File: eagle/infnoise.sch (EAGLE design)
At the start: 27 parts, among them SW1 MC74VHC1G66DFT1G, SW2 MC74VHC1G66DFT1G, X1 USBSMT-MALE

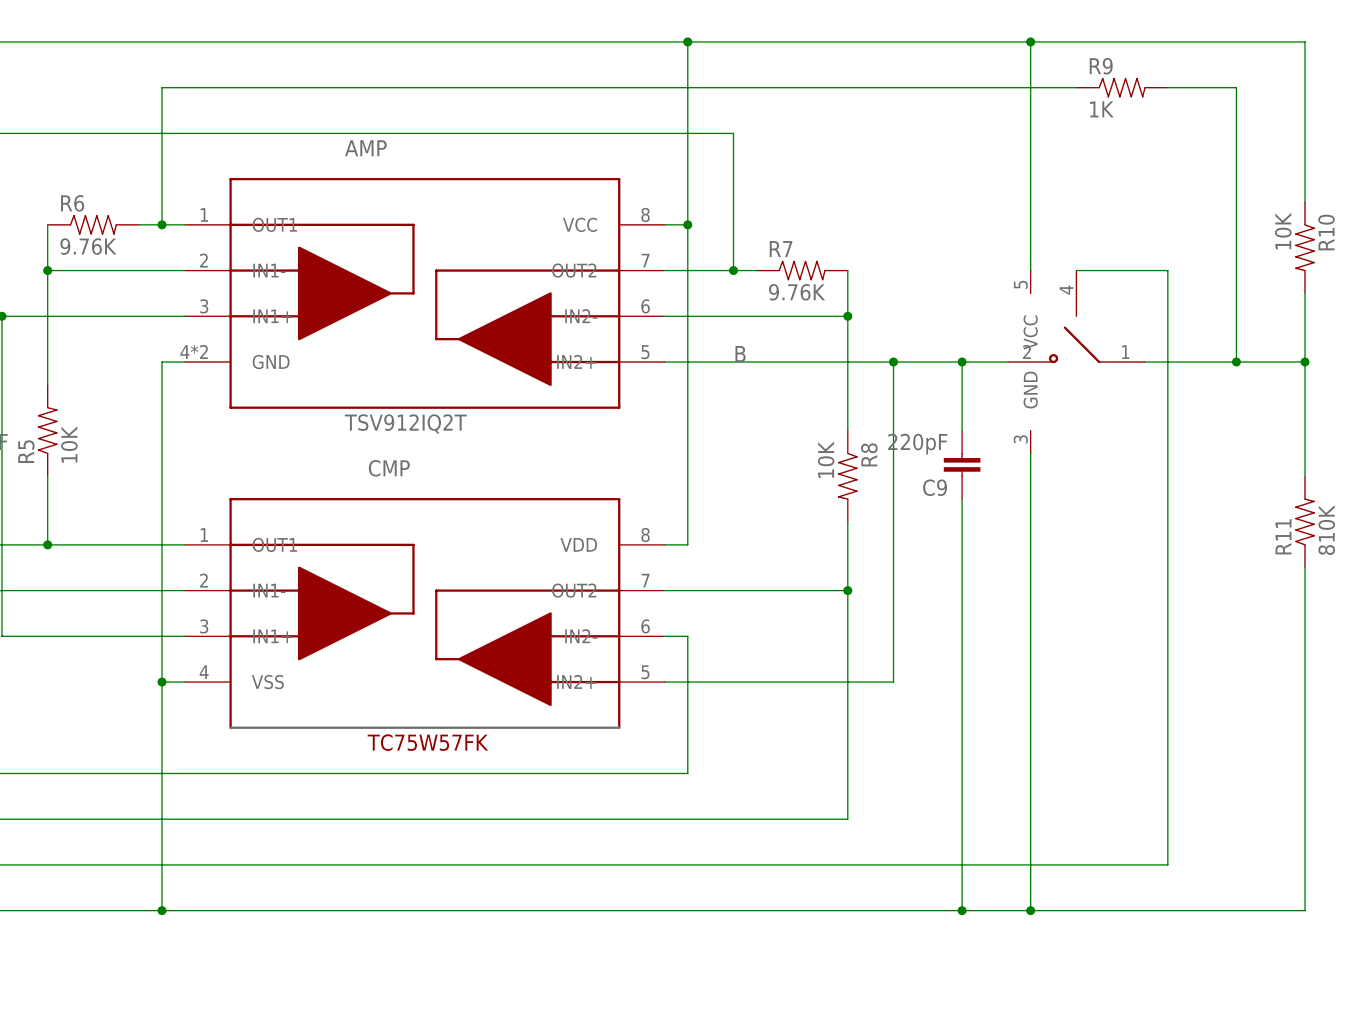
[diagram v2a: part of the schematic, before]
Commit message: Modified board to remove resistor in feedback, as well as pull-down
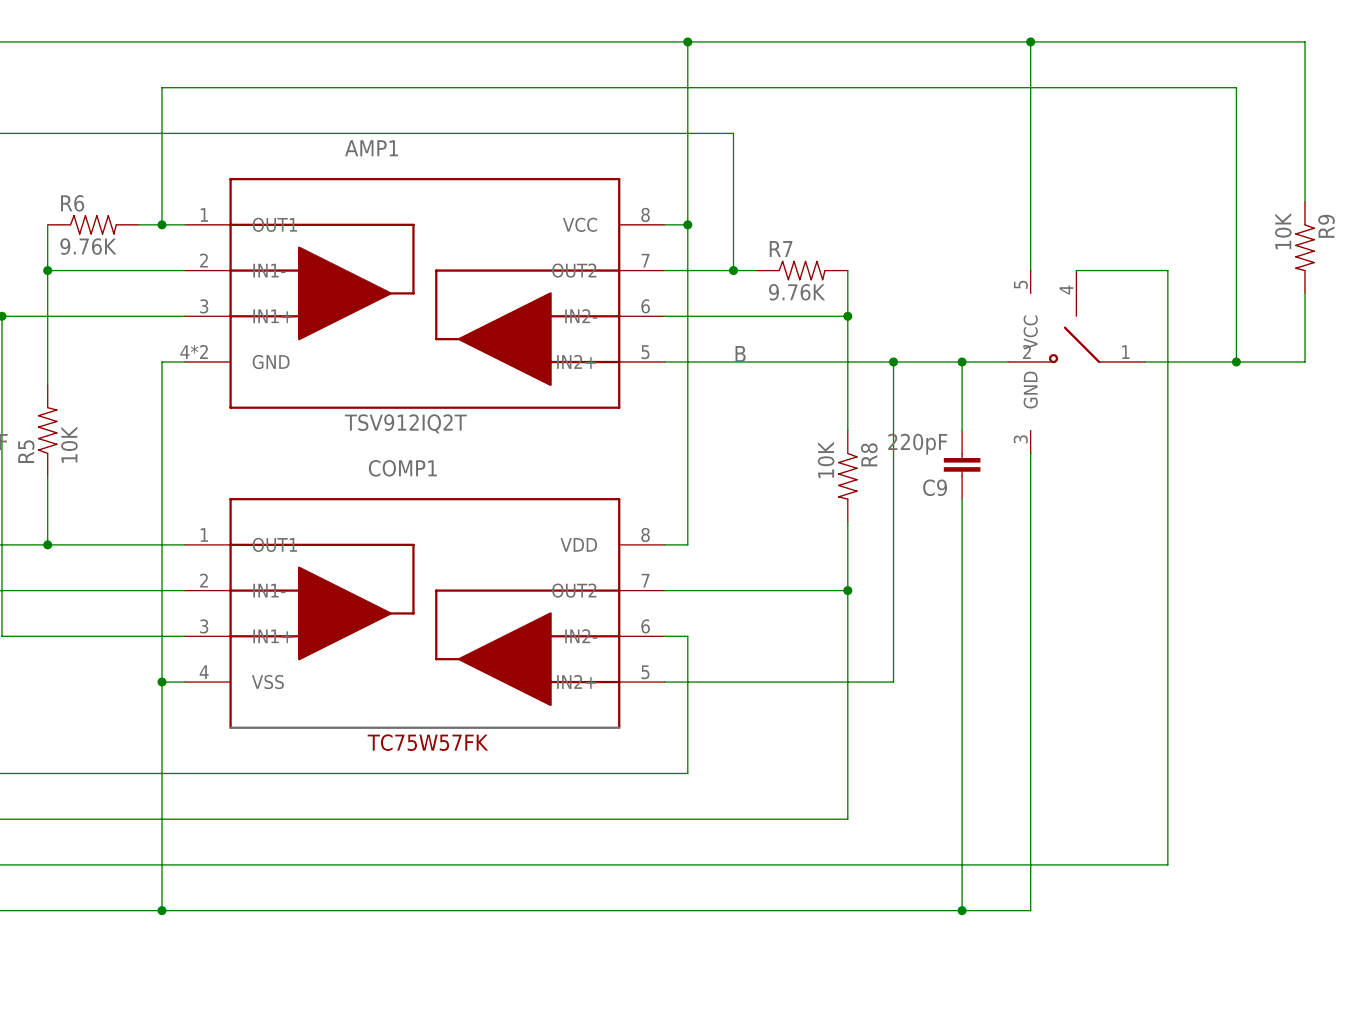
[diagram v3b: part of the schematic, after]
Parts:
- removed R10: 10K, infnoise:RESISTOR0603-RES
- removed R11: 810K, infnoise:RESISTOR0603-RES
- R9: value 1K -> 10K
- renumbered AMP to AMP1, CMP to COMP1
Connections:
- removed net N$1: AMP1.OUT1, R6.2, R9.1
- net AMP1OUT: now also AMP1.OUT1, R6.2; no longer R10.2, R11.2
- net GND: no longer R11.1
- net VCC33: now also R9.1; no longer R10.1
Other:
- moved on the sheet: R9
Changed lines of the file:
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@@
 <part name="R3" library="infnoise" deviceset="RESISTOR" device="0603-RES" value="10K"/>
 <part name="R4" library="infnoise" deviceset="RESISTOR" device="0603-RES" value="10K"/>
-<part name="AMP" library="infnoise" deviceset="TSV912" device="IQ2T"/>
-<part name="CMP" library="infnoise" deviceset="TC75W57" device="FK"/>
+<part name="AMP1" library="infnoise" deviceset="TSV912" device="IQ2T"/>
+<part name="COMP1" library="infnoise" deviceset="TC75W57" device="FK"/>
 <part name="SUPPLY1" library="supply2" deviceset="GND" device=""/>
-<part name="R10" library="infnoise" deviceset="RESISTOR" device="0603-RES" value="10K"/>
-<part name="R11" library="infnoise" deviceset="RESISTOR" device="0603-RES" value="810K"/>
+<part name="R9" library="infnoise" deviceset="RESISTOR" device="0603-RES" value="10K"/>
 <part name="SW1" library="infnoise" deviceset="MC74VHC1G66" device="DFT1G"/>
 <part name="SW2" library="infnoise" deviceset="MC74VHC1G66" device="DFT1G"/>
 <part name="X1" library="infnoise" deviceset="USB" device="SMT-MALE"/>
-<part name="R9" library="infnoise" deviceset="RESISTOR" device="0603-RES" value="1K"/>
 <part name="C7" library="infnoise" deviceset="CAP" device="0603-CAP" value="10nF"/>
 </parts>
@@
 <instance part="R3" gate="G$1" x="119.38" y="30.48" rot="R270"/>
 <instance part="R4" gate="G$1" x="119.38" y="10.16" rot="R270"/>
-<instance part="AMP" gate="G$1" x="208.28" y="50.8"/>
-<instance part="CMP" gate="G$1" x="208.28" y="15.24"/>
+<instance part="AMP1" gate="G$1" x="208.28" y="50.8"/>
+<instance part="COMP1" gate="G$1" x="208.28" y="15.24"/>
 <instance part="SUPPLY1" gate="GND" x="66.04" y="-20.32"/>
-<instance part="R10" gate="G$1" x="307.34" y="58.42" rot="R270"/>
-<instance part="R11" gate="G$1" x="307.34" y="27.94" rot="R90"/>
+<instance part="R9" gate="G$1" x="307.34" y="58.42" rot="R270"/>
 <instance part="SW1" gate="G$1" x="142.24" y="50.8"/>
 <instance part="SW2" gate="G$1" x="281.94" y="45.72" rot="MR0"/>
 <instance part="X1" gate="G$1" x="-43.18" y="35.56" rot="R180"/>
-<instance part="R9" gate="G$1" x="287.02" y="76.2"/>
 <instance part="C7" gate="G$1" x="132.08" y="7.62"/>
 </instances>
@@
 <wire x1="154.94" y1="35.56" x2="154.94" y2="-15.24" width="0.1524" layer="91"/>
 <wire x1="147.32" y1="40.64" x2="147.32" y2="-15.24" width="0.1524" layer="91"/>
-<pinref part="AMP" gate="G$1" pin="GND"/>
+<pinref part="AMP1" gate="G$1" pin="GND"/>
 <wire x1="182.88" y1="45.72" x2="180.34" y2="45.72" width="0.1524" layer="91"/>
 <wire x1="180.34" y1="45.72" x2="180.34" y2="10.16" width="0.1524" layer="91"/>
-<pinref part="CMP" gate="G$1" pin="VSS"/>
+<pinref part="COMP1" gate="G$1" pin="VSS"/>
 <wire x1="180.34" y1="10.16" x2="180.34" y2="-15.24" width="0.1524" layer="91"/>
 <wire x1="182.88" y1="10.16" x2="180.34" y2="10.16" width="0.1524" layer="91"/>
-<wire x1="276.86" y1="-15.24" x2="307.34" y2="-15.24" width="0.1524" layer="91"/>
-<pinref part="R11" gate="G$1" pin="1"/>
-<wire x1="307.34" y1="-15.24" x2="307.34" y2="22.86" width="0.1524" layer="91"/>
 <pinref part="SW1" gate="G$1" pin="GND"/>
 <pinref part="SW2" gate="G$1" pin="GND"/>
@@
 <junction x="154.94" y="-15.24"/>
 <junction x="180.34" y="-15.24"/>
-<junction x="276.86" y="-15.24"/>
 <junction x="15.24" y="10.16"/>
 <junction x="180.34" y="10.16"/>
@@
 <wire x1="147.32" y1="60.96" x2="147.32" y2="81.28" width="0.1524" layer="91"/>
 <wire x1="147.32" y1="81.28" x2="238.76" y2="81.28" width="0.1524" layer="91"/>
-<pinref part="CMP" gate="G$1" pin="VDD"/>
+<pinref part="COMP1" gate="G$1" pin="VDD"/>
 <wire x1="238.76" y1="81.28" x2="276.86" y2="81.28" width="0.1524" layer="91"/>
 <wire x1="276.86" y1="81.28" x2="307.34" y2="81.28" width="0.1524" layer="91"/>
 <wire x1="236.22" y1="25.4" x2="238.76" y2="25.4" width="0.1524" layer="91"/>
 <wire x1="238.76" y1="25.4" x2="238.76" y2="60.96" width="0.1524" layer="91"/>
-<pinref part="AMP" gate="G$1" pin="VCC"/>
+<pinref part="AMP1" gate="G$1" pin="VCC"/>
 <wire x1="238.76" y1="60.96" x2="238.76" y2="81.28" width="0.1524" layer="91"/>
 <wire x1="236.22" y1="60.96" x2="238.76" y2="60.96" width="0.1524" layer="91"/>
@@
 <wire x1="119.38" y1="35.56" x2="119.38" y2="81.28" width="0.1524" layer="91"/>
 <junction x="119.38" y="81.28"/>
-<pinref part="R10" gate="G$1" pin="1"/>
+<pinref part="R9" gate="G$1" pin="1"/>
 <wire x1="307.34" y1="81.28" x2="307.34" y2="63.5" width="0.1524" layer="91"/>
 <label x="58.42" y="81.28" size="1.778" layer="95"/>
@@
 <net name="A" class="0">
 <segment>
-<pinref part="AMP" gate="G$1" pin="IN1+"/>
+<pinref part="AMP1" gate="G$1" pin="IN1+"/>
 <wire x1="182.88" y1="50.8" x2="162.56" y2="50.8" width="0.1524" layer="91"/>
 <pinref part="C8" gate="G$1" pin="1"/>
@@
 <wire x1="154.94" y1="50.8" x2="149.86" y2="50.8" width="0.1524" layer="91"/>
 <wire x1="154.94" y1="43.18" x2="154.94" y2="50.8" width="0.1524" layer="91"/>
-<pinref part="CMP" gate="G$1" pin="IN1+"/>
+<pinref part="COMP1" gate="G$1" pin="IN1+"/>
 <wire x1="182.88" y1="15.24" x2="162.56" y2="15.24" width="0.1524" layer="91"/>
 <wire x1="162.56" y1="15.24" x2="162.56" y2="50.8" width="0.1524" layer="91"/>
@@
 <pinref part="SW2" gate="G$1" pin="COM"/>
 <wire x1="289.56" y1="45.72" x2="299.72" y2="45.72" width="0.1524" layer="91"/>
-<pinref part="R11" gate="G$1" pin="2"/>
 <wire x1="299.72" y1="45.72" x2="307.34" y2="45.72" width="0.1524" layer="91"/>
-<wire x1="307.34" y1="33.02" x2="307.34" y2="45.72" width="0.1524" layer="91"/>
 <wire x1="299.72" y1="76.2" x2="299.72" y2="45.72" width="0.1524" layer="91"/>
 <junction x="299.72" y="45.72"/>
-<pinref part="R10" gate="G$1" pin="2"/>
+<pinref part="R9" gate="G$1" pin="2"/>
 <wire x1="307.34" y1="53.34" x2="307.34" y2="45.72" width="0.1524" layer="91"/>
-<junction x="307.34" y="45.72"/>
-<pinref part="R9" gate="G$1" pin="2"/>
-<wire x1="292.1" y1="76.2" x2="299.72" y2="76.2" width="0.1524" layer="91"/>
+<pinref part="R6" gate="G$1" pin="2"/>
+<pinref part="AMP1" gate="G$1" pin="OUT1"/>
+<wire x1="182.88" y1="60.96" x2="180.34" y2="60.96" width="0.1524" layer="91"/>
+<wire x1="180.34" y1="60.96" x2="177.8" y2="60.96" width="0.1524" layer="91"/>
+<junction x="180.34" y="60.96"/>
+<wire x1="180.34" y1="60.96" x2="180.34" y2="76.2" width="0.1524" layer="91"/>
+<wire x1="180.34" y1="76.2" x2="299.72" y2="76.2" width="0.1524" layer="91"/>
 </segment>
 </net>
 <net name="FB1" class="0">
 <segment>
-<pinref part="AMP" gate="G$1" pin="IN1-"/>
+<pinref part="AMP1" gate="G$1" pin="IN1-"/>
 <wire x1="182.88" y1="55.88" x2="167.64" y2="55.88" width="0.1524" layer="91"/>
 <wire x1="167.64" y1="55.88" x2="167.64" y2="60.96" width="0.1524" layer="91"/>
@@
 <wire x1="132.08" y1="50.8" x2="134.62" y2="50.8" width="0.1524" layer="91"/>
 <pinref part="SW1" gate="G$1" pin="COM"/>
-<pinref part="AMP" gate="G$1" pin="OUT2"/>
+<pinref part="AMP1" gate="G$1" pin="OUT2"/>
 <pinref part="R7" gate="G$1" pin="1"/>
 <wire x1="246.38" y1="55.88" x2="243.84" y2="55.88" width="0.1524" layer="91"/>
@@
 <segment>
 <pinref part="R7" gate="G$1" pin="2"/>
-<pinref part="AMP" gate="G$1" pin="IN2-"/>
+<pinref part="AMP1" gate="G$1" pin="IN2-"/>
 <wire x1="236.22" y1="50.8" x2="256.54" y2="50.8" width="0.1524" layer="91"/>
 <wire x1="256.54" y1="50.8" x2="256.54" y2="55.88" width="0.1524" layer="91"/>
@@
 <net name="B" class="0">
 <segment>
-<pinref part="AMP" gate="G$1" pin="IN2+"/>
+<pinref part="AMP1" gate="G$1" pin="IN2+"/>
 <wire x1="274.32" y1="45.72" x2="269.24" y2="45.72" width="0.1524" layer="91"/>
 <wire x1="269.24" y1="45.72" x2="261.62" y2="45.72" width="0.1524" layer="91"/>
 <wire x1="261.62" y1="45.72" x2="236.22" y2="45.72" width="0.1524" layer="91"/>
-<pinref part="CMP" gate="G$1" pin="IN2+"/>
+<pinref part="COMP1" gate="G$1" pin="IN2+"/>
 <wire x1="236.22" y1="10.16" x2="261.62" y2="10.16" width="0.1524" layer="91"/>
 <wire x1="261.62" y1="10.16" x2="261.62" y2="45.72" width="0.1524" layer="91"/>
@@
 <net name="COMP1" class="0">
 <segment>
-<pinref part="CMP" gate="G$1" pin="OUT1"/>
+<pinref part="COMP1" gate="G$1" pin="OUT1"/>
 <wire x1="182.88" y1="25.4" x2="167.64" y2="25.4" width="0.1524" layer="91"/>
 <wire x1="167.64" y1="25.4" x2="127" y2="25.4" width="0.1524" layer="91"/>
@@
 <net name="COMP2" class="0">
 <segment>
-<pinref part="CMP" gate="G$1" pin="OUT2"/>
+<pinref part="COMP1" gate="G$1" pin="OUT2"/>
 <wire x1="236.22" y1="20.32" x2="256.54" y2="20.32" width="0.1524" layer="91"/>
 <wire x1="256.54" y1="20.32" x2="256.54" y2="-5.08" width="0.1524" layer="91"/>
@@
 <net name="VREF" class="0">
 <segment>
-<pinref part="CMP" gate="G$1" pin="IN1-"/>
+<pinref part="COMP1" gate="G$1" pin="IN1-"/>
 <wire x1="182.88" y1="20.32" x2="160.02" y2="20.32" width="0.1524" layer="91"/>
 <wire x1="160.02" y1="20.32" x2="160.02" y2="0" width="0.1524" layer="91"/>
 <wire x1="160.02" y1="0" x2="238.76" y2="0" width="0.1524" layer="91"/>
 <wire x1="238.76" y1="0" x2="238.76" y2="15.24" width="0.1524" layer="91"/>
-<pinref part="CMP" gate="G$1" pin="IN2-"/>
+<pinref part="COMP1" gate="G$1" pin="IN2-"/>
 <wire x1="238.76" y1="15.24" x2="236.22" y2="15.24" width="0.1524" layer="91"/>
 <wire x1="160.02" y1="20.32" x2="132.08" y2="20.32" width="0.1524" layer="91"/>
@@
 </segment>
 </net>
-<net name="N$1" class="0">
-<segment>
-<pinref part="R6" gate="G$1" pin="2"/>
-<pinref part="AMP" gate="G$1" pin="OUT1"/>
-<wire x1="182.88" y1="60.96" x2="180.34" y2="60.96" width="0.1524" layer="91"/>
-<wire x1="180.34" y1="60.96" x2="177.8" y2="60.96" width="0.1524" layer="91"/>
-<junction x="180.34" y="60.96"/>
-<wire x1="180.34" y1="60.96" x2="180.34" y2="76.2" width="0.1524" layer="91"/>
-<pinref part="R9" gate="G$1" pin="1"/>
-<wire x1="180.34" y1="76.2" x2="281.94" y2="76.2" width="0.1524" layer="91"/>
-</segment>
-</net>

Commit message: Updated BOM
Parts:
- R6, R7: value 9.76K -> 8.2K
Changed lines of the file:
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@@
 <part name="R1" library="infnoise" deviceset="RESISTOR" device="0603-RES" value="27"/>
 <part name="R2" library="infnoise" deviceset="RESISTOR" device="0603-RES" value="27"/>
-<part name="R6" library="infnoise" deviceset="RESISTOR" device="0603-RES" value="9.76K"/>
+<part name="R6" library="infnoise" deviceset="RESISTOR" device="0603-RES" value="8.2K"/>
 <part name="R5" library="infnoise" deviceset="RESISTOR" device="0603-RES" value="10K"/>
-<part name="R7" library="infnoise" deviceset="RESISTOR" device="0603-RES" value="9.76K"/>
+<part name="R7" library="infnoise" deviceset="RESISTOR" device="0603-RES" value="8.2K"/>
 <part name="R8" library="infnoise" deviceset="RESISTOR" device="0603-RES" value="10K"/>
 <part name="R3" library="infnoise" deviceset="RESISTOR" device="0603-RES" value="10K"/>
